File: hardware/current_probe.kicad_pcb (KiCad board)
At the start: 2 copper layers, 50 x 20 mm, 74 parts, among them J1 SMA, J2 Conn_01x02_Pin, J3 Conn_01x05_Pin, U1 AD8331ARQZ, U2 ADR510ARTZ, U3 ADM7150ARDZ-5.0

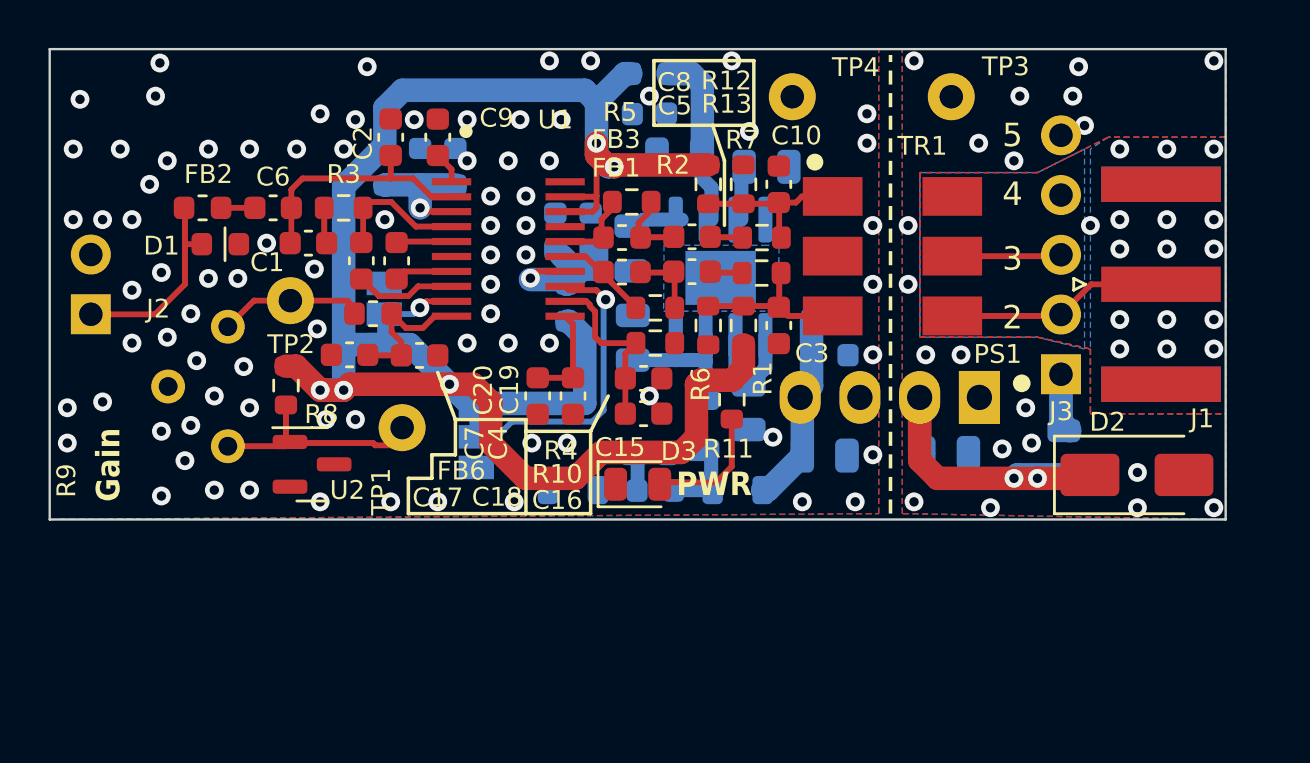
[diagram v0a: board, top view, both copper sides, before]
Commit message: Incorporate design review feedback - Enhance routing of input path - Remove voltage reference, used voltage divider instead for gain voltage - Made vias smaller
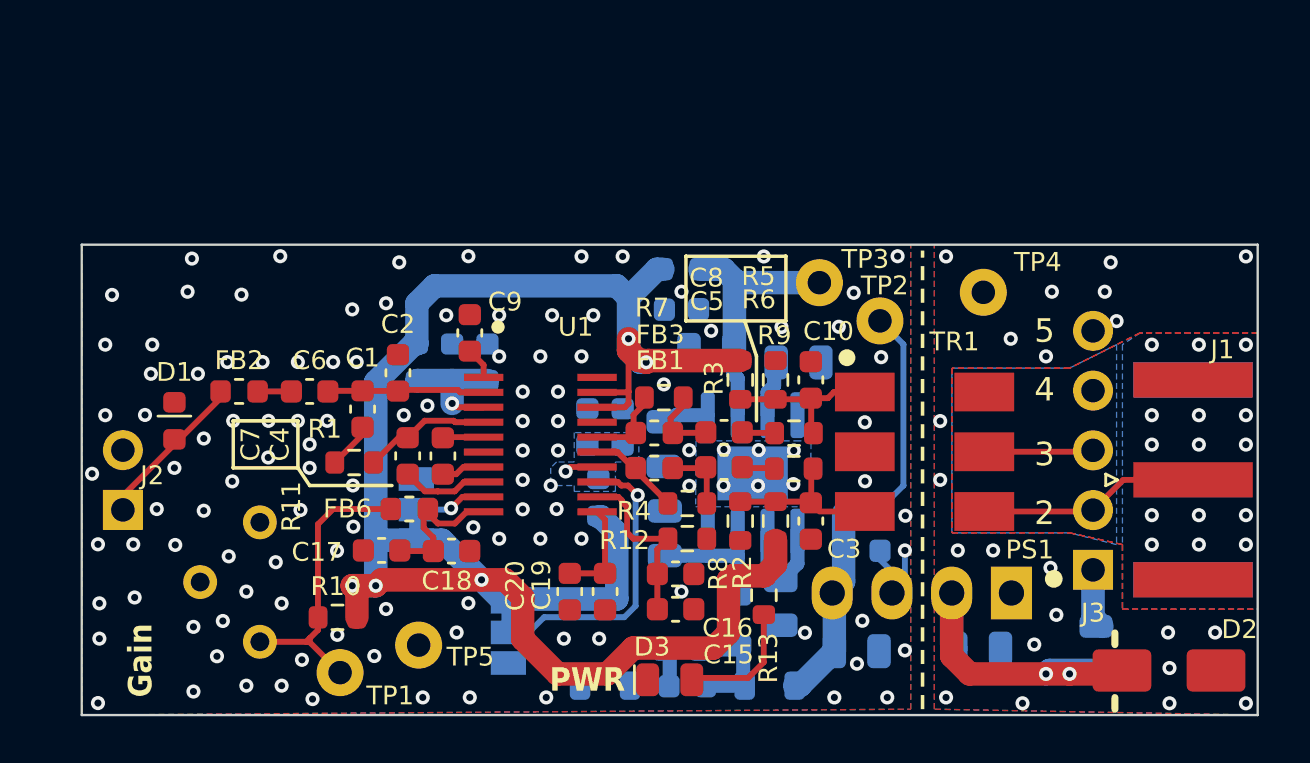
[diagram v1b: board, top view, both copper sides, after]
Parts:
- removed the TP1 at (135.5, 103.4)
- removed the U2 at (131.7, 104.9)
- added TP2: TestPoint, TestPoint:TestPoint_Loop_D1.80mm_Drill1.0mm_Beaded, F.Cu at (155.9, 98.8)
- added TP3: TestPoint, TestPoint:TestPoint_Loop_D1.80mm_Drill1.0mm_Beaded, F.Cu at (153.3, 97.2)
- D3: value LED -> GREEN
- F1: value 250mA -> 300 mA
- FB1, FB2, FB3: value BLM21 -> 22
- FB4, FB5, FB6, FB7: value BLM21 -> 2k2
- R10: renamed from R8; value 4k7 -> 12k
- R11: renamed from R9; value 4k7 -> 3k
- moved TP5 28.2 mm to (136.2, 112.6)
- moved TP1 16.0 mm to (132.9, 113.8)
- moved R1 10.8 mm to (133.5, 104.8)
- moved R10 10.1 mm to (132.8, 111.4), turned to 180 degrees
- moved C2 10.0 mm to (135.4, 101.0)
- moved C4 8.53 mm to (137.3, 104.6)
- moved C7 8.53 mm to (135.8, 104.6)
- moved FB1 8.45 mm to (146.3, 105.1), turned to 180 degrees
- moved FB6 8.45 mm to (135.9, 106.8)
- moved C18 8.43 mm to (137.6, 108.6)
- moved C25 8.43 mm to (147.7, 114.4)
- moved C26 8.43 mm to (147.4, 112.8)
- moved C28 8.43 mm to (148.7, 100.1)
- moved C29 8.43 mm to (148.9, 98.3)
- moved C30 8.43 mm to (145.9, 98.3)
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- renumbered C32 to C31, C33 to C32, C31 to C33, R3 to R1, R10 to R12, R11 to R13, R1 to R2, R2 to R3, R12 to R5, R13 to R6, R5 to R7, R6 to R8, R7 to R9, TP2 to TP1, TP3 to TP4, TP4 to TP5, U3 to U2
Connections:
- C28 pad 2: Net-(U3-VOUT) -> Net-(U2-VOUT)
- C29 pad 2: Net-(U3-VOUT) -> Net-(U2-VOUT)
- FB1 pad 1: Net-(FB1-Pad1) -> Net-(C5-Pad2)
- FB1 pad 2: Net-(C5-Pad2) -> Net-(FB1-Pad2)
- FB7 pad 1: Net-(U3-VOUT) -> +5V
- FB7 pad 2: +5V -> Net-(U2-VOUT)
- R10 pad 2: Net-(U2-K) -> Net-(FB6-Pad2)
- R11 pad 1: Net-(U2-K) -> Net-(FB6-Pad2)
- R11 pad 3: Net-(FB6-Pad2) -> GND
- R4 pad 1: Net-(FB1-Pad1) -> Net-(FB1-Pad2)
- U1 pad 15: Net-(FB1-Pad1) -> Net-(FB1-Pad2)
- U2 pad 2: Net-(U3-VOUT) -> Net-(U2-VOUT)
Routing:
- net Net-(U2-VOUT): track 0.00 -> 11.2 mm
- net +9V: track 8.19 -> 18.7 mm
- net Net-(U2-K): track 9.19 -> 0.00 mm
- net Net-(U3-VOUT): track 7.59 -> 0.00 mm
- net Net-(FB6-Pad2): track 6.33 -> 12.5 mm
- net Net-(U1D-VPOS): track 6.70 -> 1.42 mm
- net GND: track 0.00 -> 4.04 mm, vias 82 -> 119
- net Net-(FB1-Pad2): track 0.00 -> 3.94 mm
- net Net-(FB1-Pad1): track 3.94 -> 0.00 mm
- net Net-(U1A-+): track 10.6 -> 6.69 mm
- net Net-(D1-A1): track 8.53 -> 6.76 mm
- net Net-(C4-Pad2): track 2.35 -> 1.74 mm
- net Net-(U1C-+): track 2.47 -> 1.86 mm
- net Net-(U1C--): track 4.31 -> 3.70 mm
- net Net-(J1-Ext): vias 16 -> 15
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- added copper zone on B.Cu, net Net-(U1D-VPOS)

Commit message: Updated BOM and part numbers
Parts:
- D1: value EZA-EG2N50AX -> 2.5 pF
- R4, R7: value 330 -> 100
- TR1: value ADTT1-6 -> ADTT1-6+
